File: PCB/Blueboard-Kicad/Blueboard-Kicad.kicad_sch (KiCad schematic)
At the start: 130 parts, among them SW1 M1, SW10 SHIFT, SW11 CTL, SW12 1, SW13 Q, SW14 A, SW15 Z, SW16 WIN, SW17 F1, SW18 2, SW19 W, SW2 ESC, SW20 S, SW21 X, SW22 ALT, SW23 F2, SW24 3, SW25 E, SW26 D, SW27 C, SW28 F3, SW29 4, SW3 M1, SW30 R, SW31 F, SW32 V, SW33 F4, SW34 5, SW35 T, SW36 G, SW37 B, SW38 SPACE, SW39 6, SW4 M1, SW40 Y, SW41 H, SW42 N, SW43 7, SW44 U, SW45 J, SW46 M, SW47 F5, SW48 F6, SW49 8, SW5 M1, SW50 I, SW51 K, SW52 <, SW53 ALT, SW54 F7, SW55 9, SW56 O, SW57 L, SW58 >, SW59 WIN, SW6 M1, SW60 F8, SW61 0, SW62 P, SW63 ;, SW64 ?, SW65 Menu, SW7 TILDA, SW8 TAB, SW9 CAPS

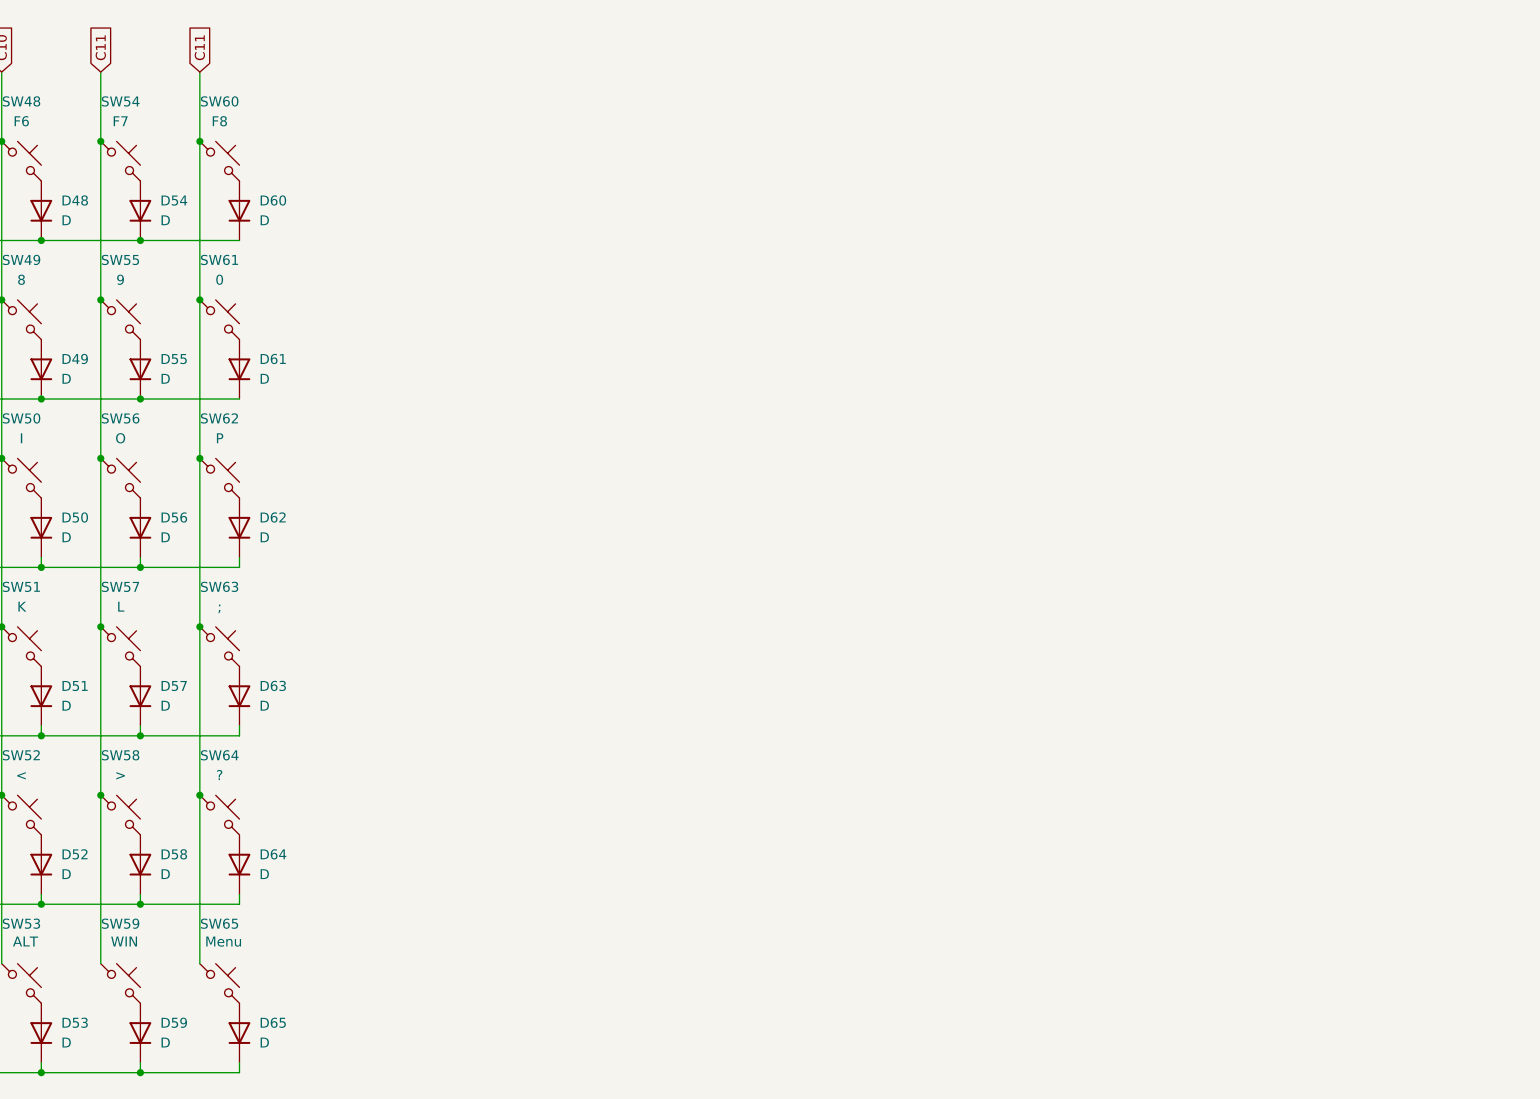
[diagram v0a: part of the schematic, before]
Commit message: Updated Schematic With Completed Matrix
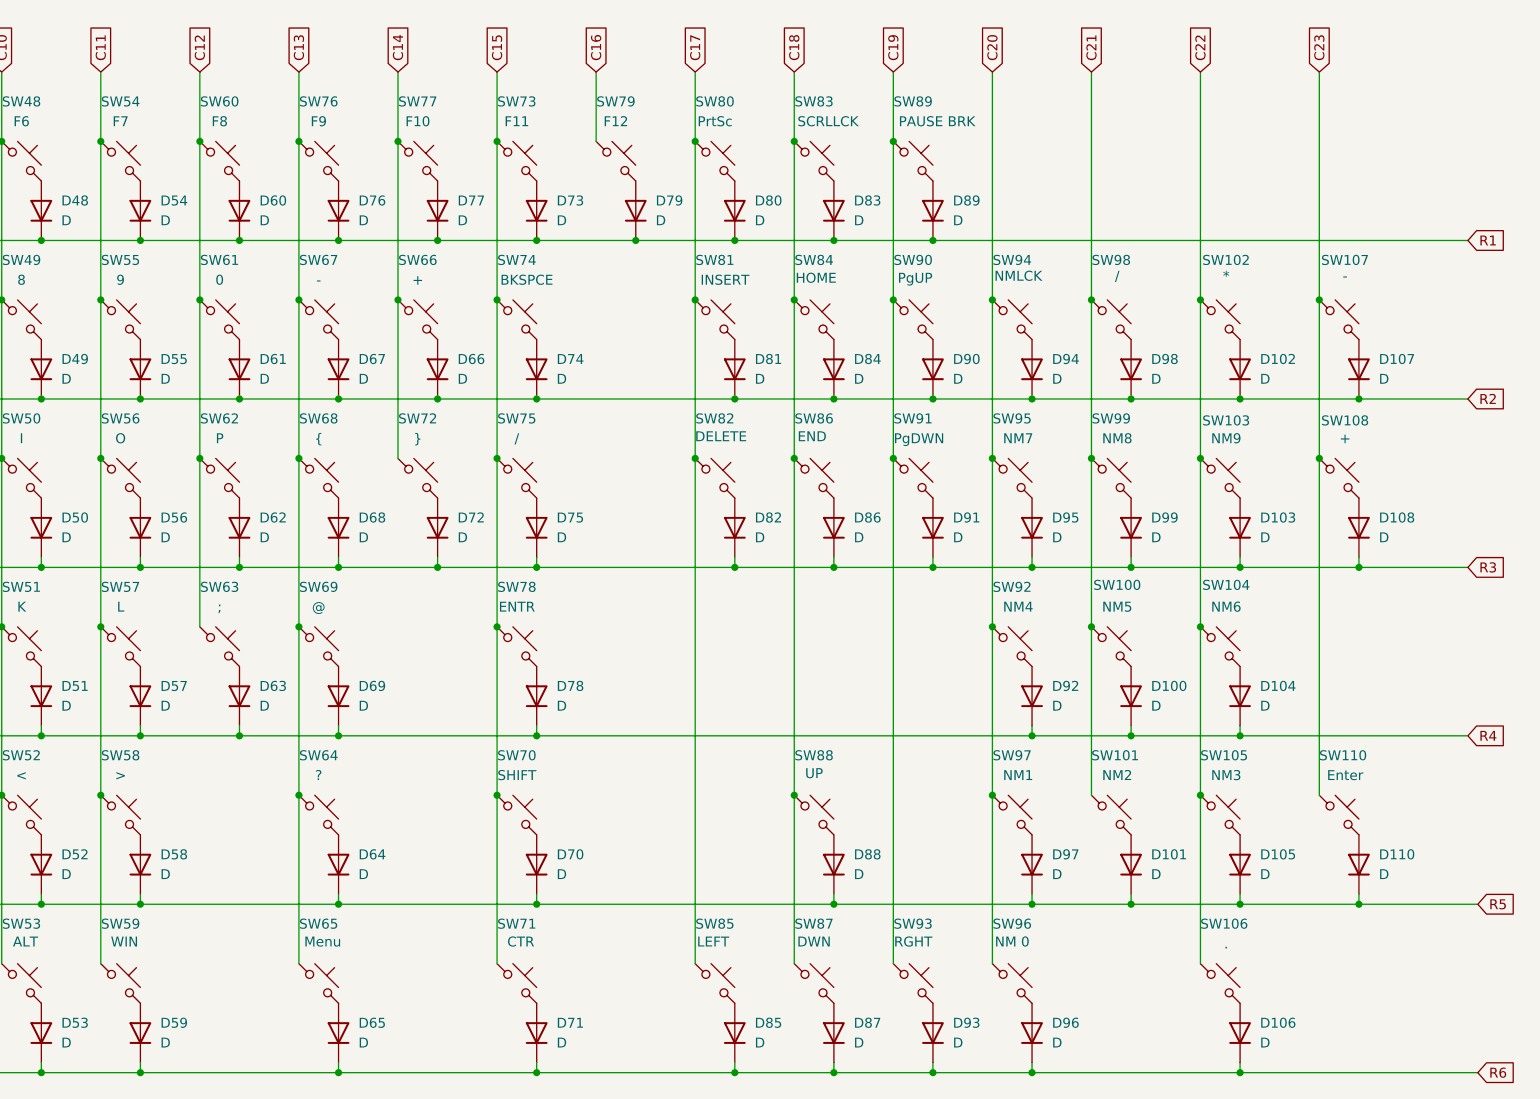
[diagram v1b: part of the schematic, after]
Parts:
- added D100, D101, D102, D103, D104, D105, D106, D107, D108, D110, D66, D67, D68, D69, D70, D71, D72, D73, D74, D75, D76, D77, D78, D79, D80, D81, D82, D83, D84, D85, D86, D87, D88, D89, D90, D91, D92, D93, D94, D95, D96, D97, D98, D99: D, symbol Device:D
- added SW100: NM5, symbol Switch:SW_Push_45deg
- added SW101: NM2, symbol Switch:SW_Push_45deg
- added SW102: *, symbol Switch:SW_Push_45deg
- added SW103: NM9, symbol Switch:SW_Push_45deg
- added SW104: NM6, symbol Switch:SW_Push_45deg
- added SW105: NM3, symbol Switch:SW_Push_45deg
- added SW106: ., symbol Switch:SW_Push_45deg
- added SW107, SW67: -, symbol Switch:SW_Push_45deg
- added SW108, SW66: +, symbol Switch:SW_Push_45deg
- added SW110: Enter, symbol Switch:SW_Push_45deg
- added SW68: {, symbol Switch:SW_Push_45deg
- added SW69: @, symbol Switch:SW_Push_45deg
- added SW70: SHIFT, symbol Switch:SW_Push_45deg
- added SW71: CTR, symbol Switch:SW_Push_45deg
- added SW72: }, symbol Switch:SW_Push_45deg
- added SW73: F11, symbol Switch:SW_Push_45deg
- added SW74: BKSPCE, symbol Switch:SW_Push_45deg
- added SW75, SW98: /, symbol Switch:SW_Push_45deg
- added SW76: F9, symbol Switch:SW_Push_45deg
- added SW77: F10, symbol Switch:SW_Push_45deg
- added SW78: ENTR, symbol Switch:SW_Push_45deg
- added SW79: F12, symbol Switch:SW_Push_45deg
- added SW80: PrtSc, symbol Switch:SW_Push_45deg
- added SW81: INSERT, symbol Switch:SW_Push_45deg
- added SW82: DELETE, symbol Switch:SW_Push_45deg
- added SW83: SCRLLCK, symbol Switch:SW_Push_45deg
- added SW84: HOME, symbol Switch:SW_Push_45deg
- added SW85: LEFT, symbol Switch:SW_Push_45deg
- added SW86: END, symbol Switch:SW_Push_45deg
- added SW87: DWN, symbol Switch:SW_Push_45deg
- added SW88: UP, symbol Switch:SW_Push_45deg
- added SW89: PAUSE BRK, symbol Switch:SW_Push_45deg
- added SW90: PgUP, symbol Switch:SW_Push_45deg
- added SW91: PgDWN, symbol Switch:SW_Push_45deg
- added SW92: NM4, symbol Switch:SW_Push_45deg
- added SW93: RGHT, symbol Switch:SW_Push_45deg
- added SW94: NMLCK, symbol Switch:SW_Push_45deg
- added SW95: NM7, symbol Switch:SW_Push_45deg
- added SW96: NM 0, symbol Switch:SW_Push_45deg
- added SW97: NM1, symbol Switch:SW_Push_45deg
- added SW99: NM8, symbol Switch:SW_Push_45deg
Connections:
- net C11: no longer SW60.1, SW61.1, SW62.1, SW63.1, SW64.1, SW65.1
- net R3: now reaches D13.1 (K), D19.1 (K), D25.1 (K), D3.1 (K), D30.1 (K), D35.1 (K), D40.1 (K), D44.1 (K), D50.1 (K), D56.1 (K), D62.1 (K), D8.1 (K)
- net R3: now also D103.1 (K), D108.1 (K), D68.1 (K), D72.1 (K), D75.1 (K), D82.1 (K), D86.1 (K), D91.1 (K), D95.1 (K), D99.1 (K)
- net R4: now reaches D14.1 (K), D20.1 (K), D26.1 (K), D31.1 (K), D36.1 (K), D4.1 (K), D41.1 (K), D45.1 (K), D51.1 (K), D57.1 (K), D63.1 (K), D9.1 (K)
- net R4: now also D100.1 (K), D104.1 (K), D69.1 (K), D78.1 (K), D92.1 (K)
- net R2: now reaches D1.1 (K), D12.1 (K), D18.1 (K), D24.1 (K), D29.1 (K), D34.1 (K), D39.1 (K), D43.1 (K), D49.1 (K), D55.1 (K), D61.1 (K), D7.1 (K)
- net R2: now also D102.1 (K), D107.1 (K), D66.1 (K), D67.1 (K), D74.1 (K), D81.1 (K), D84.1 (K), D90.1 (K), D94.1 (K), D98.1 (K)
- net R1: now reaches D17.1 (K), D2.1 (K), D23.1 (K), D28.1 (K), D33.1 (K), D47.1 (K), D48.1 (K), D54.1 (K), D60.1 (K)
- net R1: now also D73.1 (K), D76.1 (K), D77.1 (K), D79.1 (K), D80.1 (K), D83.1 (K), D89.1 (K)
- net R5: now reaches D10.1 (K), D15.1 (K), D21.1 (K), D27.1 (K), D32.1 (K), D37.1 (K), D42.1 (K), D46.1 (K), D5.1 (K), D52.1 (K), D58.1 (K), D64.1 (K)
- net R5: now also D101.1 (K), D105.1 (K), D110.1 (K), D70.1 (K), D88.1 (K), D97.1 (K)
- net R6: now reaches D11.1 (K), D16.1 (K), D22.1 (K), D38.1 (K), D53.1 (K), D59.1 (K), D6.1 (K), D65.1 (K)
- net R6: now also D106.1 (K), D71.1 (K), D85.1 (K), D87.1 (K), D93.1 (K), D96.1 (K)
- new net: D105.2 (A), SW105.2
- new net: D110.2 (A), SW110.2
- new net: D103.2 (A), SW103.2
- new net: D94.2 (A), SW94.2
- new net: D92.2 (A), SW92.2
- new net: D73.2 (A), SW73.2
- new net: D88.2 (A), SW88.2
- new net: D97.2 (A), SW97.2
- new net: D85.2 (A), SW85.2
- new net: D80.2 (A), SW80.2
- new net: D89.2 (A), SW89.2
- new net: D81.2 (A), SW81.2
- new net: D106.2 (A), SW106.2
- new net: D83.2 (A), SW83.2
- new net: D70.2 (A), SW70.2
- new net: D108.2 (A), SW108.2
- new net: D77.2 (A), SW77.2
- new net: D93.2 (A), SW93.2
- new net: D86.2 (A), SW86.2
- new net: D68.2 (A), SW68.2
- new net: D101.2 (A), SW101.2
- new net: D69.2 (A), SW69.2
- new net: D102.2 (A), SW102.2
- new net: D74.2 (A), SW74.2
- new net: D107.2 (A), SW107.2
- new net: D66.2 (A), SW66.2
- new net: D71.2 (A), SW71.2
- new net: D75.2 (A), SW75.2
- new net: D90.2 (A), SW90.2
- new net: D82.2 (A), SW82.2
- new net: D95.2 (A), SW95.2
- new net: D104.2 (A), SW104.2
- new net: D96.2 (A), SW96.2
- new net: D91.2 (A), SW91.2
- new net: D72.2 (A), SW72.2
- new net: D87.2 (A), SW87.2
- new net: D100.2 (A), SW100.2
- new net: D98.2 (A), SW98.2
- new net: D79.2 (A), SW79.2
- new net: D78.2 (A), SW78.2
- new net: D99.2 (A), SW99.2
- new net: D76.2 (A), SW76.2
- new net: D67.2 (A), SW67.2
- new net: D84.2 (A), SW84.2
- new net C12: SW60.1, SW61.1, SW62.1, SW63.1
- new net C13: SW64.1, SW65.1, SW67.1, SW68.1, SW69.1, SW76.1
- new net C14: SW66.1, SW72.1, SW77.1
- new net C15: SW70.1, SW71.1, SW73.1, SW74.1, SW75.1, SW78.1
- new net C16: SW79.1
- new net C17: SW80.1, SW81.1, SW82.1, SW85.1
- new net C18: SW83.1, SW84.1, SW86.1, SW87.1, SW88.1
- new net C19: SW89.1, SW90.1, SW91.1, SW93.1
- new net C20: SW92.1, SW94.1, SW95.1, SW96.1, SW97.1
- new net C21: SW100.1, SW101.1, SW98.1, SW99.1
- new net C22: SW102.1, SW103.1, SW104.1, SW105.1, SW106.1
- new net C23: SW107.1, SW108.1, SW110.1
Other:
- moved on the sheet: D64, D65, SW64, SW65

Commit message: Finished Schematc + Layedout Components
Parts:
- added J1: OLED, KiCad-SSD1306-0.91-OLED-4pin-128x32:SSD1306-0.91-OLED-4pin-128x32, symbol Connector:Conn_01x04_Socket
- added SW109, SW111: RotaryEncoder_Switch, Rotary_Encoder:RotaryEncoder_Alps_EC11E-Switch_Vertical_H20mm_MountingHoles, symbol Device:RotaryEncoder_Switch
- added U1: XIAO-ESP32-C3-DIP, Seeed Studio XIAO Series Library:XIAO-ESP32C3-DIP, symbol Seeed_Studio_XIAO_Series:XIAO-ESP32-C3-DIP
- added U3, U4: MCP23017_SP, Package_DIP:DIP-28_W7.62mm, symbol Interface_Expansion:MCP23017_SP
- D1, D10, D100, D101, D102, D103, D104, D105, D106, D107, D108, D11, D110, D12, D13, D14, D15, D16, D17, D18, D19, D2, D20, D21, D22, D23, D24, D25, D26, D27, D28, D29, D3, D30, D31, D32, D33, D34, D35, D36, D37, D38, D39, D4, D40, D41, D42, D43, D44, D45, D46, D47, D48, D49, D5, D50, D51, D52, D53, D54, D55, D56, D57, D58, D59, D6, D60, D61, D62, D63, D64, D65, D66, D67, D68, D69, D7, D70, D71, D72, D73, D74, D75, D76, D77, D78, D79, D8, D80, D81, D82, D83, D84, D85, D86, D87, D88, D89, D9, D90, D91, D92, D93, D94, D95, D96, D97, D98, D99: footprint (none) -> Diode_THT:D_DO-41_SOD81_P7.62mm_Horizontal
- SW1, SW100, SW101, SW102, SW103, SW104, SW105, SW106, SW107, SW12, SW13, SW14, SW15, SW17, SW18, SW19, SW2, SW20, SW21, SW23, SW24, SW25, SW26, SW27, SW28, SW29, SW30, SW31, SW32, SW33, SW34, SW35, SW36, SW37, SW39, SW40, SW41, SW42, SW43, SW44, SW45, SW46, SW47, SW48, SW49, SW50, SW51, SW52, SW54, SW55, SW56, SW57, SW58, SW60, SW61, SW62, SW63, SW64, SW66, SW67, SW68, SW69, SW7, SW76, SW77, SW79, SW80, SW81, SW82, SW83, SW84, SW85, SW86, SW87, SW88, SW89, SW90, SW91, SW92, SW93, SW94, SW95, SW97, SW98, SW99: footprint (none) -> Keyboard:SW_Cherry_MX1A_1.00u_PCB
- SW10, SW78: footprint (none) -> Keyboard:SW_Cherry_MX1A_2.25u_PCB
- SW108, SW110: footprint (none) -> Keyboard:SW_Cherry_MX1A_2.00u_Vertical_PCB
- SW11, SW16, SW22, SW53, SW59, SW65, SW71, SW72, SW73: footprint (none) -> Keyboard:SW_Cherry_MX1A_1.25u_PCB
- SW3: value M1 -> M2; footprint (none) -> Keyboard:SW_Cherry_MX1A_1.00u_PCB
- SW38: footprint (none) -> Keyboard:SW_Cherry_MX1A_6.25u_PCB
- SW4: value M1 -> M3; footprint (none) -> Keyboard:SW_Cherry_MX1A_1.00u_PCB
- SW5: value M1 -> M4; footprint (none) -> Keyboard:SW_Cherry_MX1A_1.00u_PCB
- SW6: value M1 -> M5; footprint (none) -> Keyboard:SW_Cherry_MX1A_1.00u_PCB
- SW70: footprint (none) -> Keyboard:SW_Cherry_MX1A_2.75u_PCB
- SW74, SW96: footprint (none) -> Keyboard:SW_Cherry_MX1A_2.00u_PCB
- SW75, SW8: footprint (none) -> Keyboard:SW_Cherry_MX1A_1.50u_PCB
- SW9: footprint (none) -> Keyboard:SW_Cherry_MX1A_1.75u_PCB
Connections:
- net C1: now also U4.1 (GPB0)
- net C10: now also U4.22 (GPA1)
- net C11: now also U4.23 (GPA2)
- net C12: now also U4.24 (GPA3)
- net C13: now also U4.25 (GPA4)
- net C14: now also U4.26 (GPA5)
- net C15: now also U4.27 (GPA6)
- net C16: now also U4.28 (GPA7)
- net C17: now also U3.1 (GPB0)
- net C18: now also U3.2 (GPB1)
- net C19: now also U3.3 (GPB2)
- net C2: now also U4.2 (GPB1)
- net C20: now also U3.4 (GPB3)
- net C21: now also U3.5 (GPB4)
- net C22: now also U3.6 (GPB5)
- net C23: now also U3.7 (GPB6)
- net C3: now also U4.3 (GPB2)
- net C4: now also U4.4 (GPB3)
- net C5: now also U4.5 (GPB4)
- net C6: now also U4.6 (GPB5)
- net C7: now also U4.7 (GPB6)
- net C8: now also U4.8 (GPB7)
- net C9: now also U4.21 (GPA0)
- net R1: now also U3.21 (GPA0)
- net R2: now also U3.22 (GPA1)
- net R3: now also U3.23 (GPA2)
- net R4: now also U3.24 (GPA3)
- net R5: now also U3.25 (GPA4)
- net R6: now also U3.26 (GPA5)
- new net ENC1_A: SW111.B, U1.8 (GPIO20/D7/RX)
- new net ENC1_B: SW111.A, U1.9 (GPIO8/D8/SCK)
- new net ENC1_SW: SW111.S1, U1.2 (GPIO3/A1/D1)
- new net ENC2_A: SW109.A, U1.10 (GPIO9/D9/MISO)
- new net ENC2_B: SW109.B, U1.11 (GPIO10/D10/MOSI)
- new net ENC2_SW: SW109.S1, U1.1 (GPIO2/A0/D0)
- new net GND: J1.1 (Pin_1), SW109.C, SW109.S2, SW111.C, SW111.S2, U1.13 (GND), U3.10 (VSS), U3.16 (A1), U3.17 (A2), U4.10 (VSS), U4.15 (A0), U4.16 (A1), U4.17 (A2)
- new net SCL: J1.3 (Pin_3), U1.6 (GPIO7/D5/SCL), U3.12 (SCK), U4.12 (SCK)
- new net SDA: J1.4 (Pin_4), U1.5 (GPIO6/D4/SDA), U3.13 (SDA), U4.13 (SDA)
- new net VCC: J1.2 (Pin_2), U1.12 (VCC_3V3), U3.15 (A0), U3.18 (~{RESET}), U3.9 (VDD), U4.18 (~{RESET}), U4.9 (VDD)
- no-connect marks 0 -> 11
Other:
- note added: "GIPO Expanders"
- note added: "Key Matrix"
- note added: "Marvel Cinematic Universe"
- note added: "OLED"
- note added: "Rotary Encoder Switches"

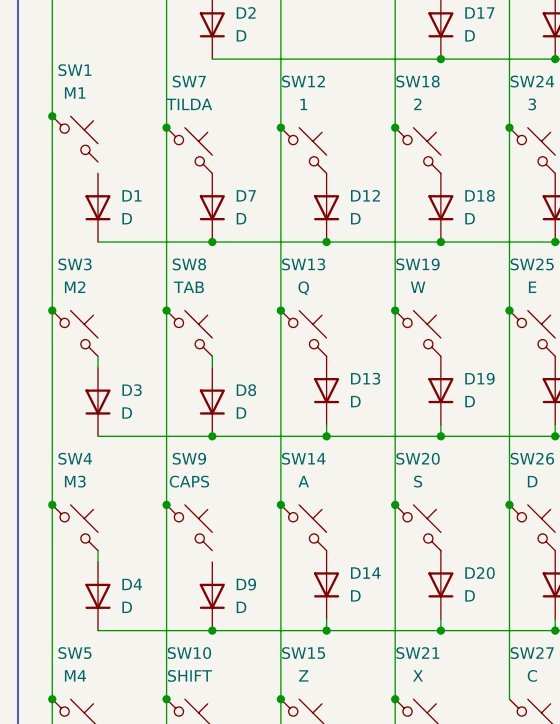
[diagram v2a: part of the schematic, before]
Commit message: Started Adding the Diodes to the PCB
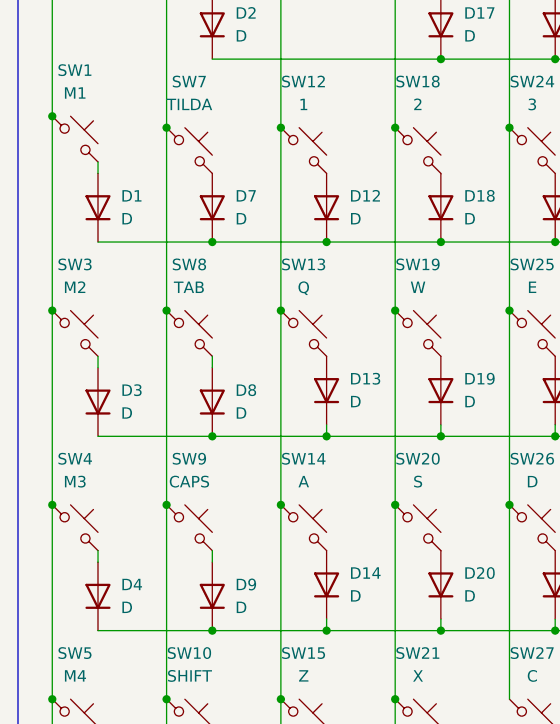
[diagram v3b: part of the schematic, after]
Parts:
- SW75: footprint Keyboard:SW_Cherry_MX1A_1.50u_PCB -> Keyboard:SW_Cherry_MX1A_1.00u_PCB
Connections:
- net at SW9.2: now also D9.2 (A)
- net at D1.2 (A): now also SW1.2
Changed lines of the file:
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@@
 	(wire
 		(pts
+			(xy 35.56 97.79) (xy 35.56 99.06)
+		)
+		(stroke
+			(width 0)
+			(type default)
+		)
+	)
+	(wire
+		(pts
 			(xy 99.06 148.59) (xy 99.06 149.86)
 		)
@@
 	(wire
 		(pts
+			(xy 22.86 54.61) (xy 22.86 55.88)
+		)
+		(stroke
+			(width 0)
+			(type default)
+		)
+	)
+	(wire
+		(pts
 			(xy 43.18 114.3) (xy 43.18 135.89)
 		)
@@
 			)
 		)
-		(property "Footprint" "Keyboard:SW_Cherry_MX1A_1.50u_PCB"
+		(property "Footprint" "Keyboard:SW_Cherry_MX1A_1.00u_PCB"
 			(at 198.12 73.66 0)
 			(effects

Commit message: Forgot to Commit PCB Changes
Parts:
- SW52: renamed from SW72; footprint Keyboard:SW_Cherry_MX1A_1.25u_PCB -> Keyboard:SW_Cherry_MX1A_1.00u_PCB
- SW53: renamed from SW75; footprint Keyboard:SW_Cherry_MX1A_1.00u_PCB -> Keyboard:SW_Cherry_MX1A_1.25u_PCB
- renumbered SW109 to ROT2, SW111 to ROT3, SW2 to SW1, SW76 to SW10, SW38 to SW100, SW53 to SW101, SW59 to SW102, SW65 to SW103, SW71 to SW104, SW85 to SW105, SW87 to SW106, SW93 to SW107, SW96 to SW108, SW106 to SW109, SW77 to SW11, SW73 to SW12, SW79 to SW13, SW80 to SW14, SW83 to SW15, SW89 to SW16, SW1 to SW17, SW7 to SW18, SW12 to SW19, SW17 to SW2, SW18 to SW20, SW24 to SW21, SW29 to SW22, SW34 to SW23, SW39 to SW24, SW43 to SW25, SW49 to SW26, SW55 to SW27, SW61 to SW28, SW67 to SW29, SW23 to SW3, SW66 to SW30, SW74 to SW31, SW81 to SW32, SW84 to SW33, SW90 to SW34, SW94 to SW35, SW98 to SW36, SW102 to SW37, SW107 to SW38, SW3 to SW39, SW28 to SW4, SW8 to SW40, SW13 to SW41, SW19 to SW42, SW25 to SW43, SW30 to SW44, SW35 to SW45, SW40 to SW46, SW44 to SW47, SW50 to SW48, SW56 to SW49, SW33 to SW5, SW62 to SW50, SW68 to SW51, SW82 to SW54, SW86 to SW55, SW91 to SW56, SW95 to SW57, SW99 to SW58, SW103 to SW59, SW47 to SW6, SW108 to SW60, SW4 to SW61, SW9 to SW62, SW14 to SW63, SW20 to SW64, SW26 to SW65, SW31 to SW66, SW36 to SW67, SW41 to SW68, SW45 to SW69, SW48 to SW7, SW51 to SW70, SW57 to SW71, SW63 to SW72, SW69 to SW73, SW78 to SW74, SW92 to SW75, SW100 to SW76, SW104 to SW77, SW5 to SW78, SW10 to SW79, SW54 to SW8, SW15 to SW80, SW21 to SW81, SW27 to SW82, SW32 to SW83, SW37 to SW84, SW42 to SW85, SW46 to SW86, SW52 to SW87, SW58 to SW88, SW64 to SW89, SW60 to SW9, SW70 to SW90, SW88 to SW91, SW97 to SW92, SW101 to SW93, SW105 to SW94, SW110 to SW95, SW6 to SW96, SW11 to SW97, SW16 to SW98, SW22 to SW99
